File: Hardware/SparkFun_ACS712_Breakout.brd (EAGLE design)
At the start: 24.1 x 15.2 mm, 12 parts, among them U1 ACS712

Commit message: A few more QC clean ups
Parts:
- added U$1: REVISION, SparkFun-Aesthetics:REVISION
- JP1, JP2: value M01-SMTSO-256-ET -> (none); device SparkFun:SMTSO-256-ET -> SparkFun-Connectors:SMTSO-256-ET
- JP3: device SparkFun:1X04 -> SparkFun-Connectors:1X04
- JP4, JP5: device SparkFun:MICRO-FIDUCIAL -> SparkFun-Aesthetics:MICRO-FIDUCIAL
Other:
- board text added: "P. Alberts, Toni Klopfenstein"
- board text removed: "Revised by: Patrick Alberts"
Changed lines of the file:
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@@
 <?xml version="1.0" encoding="utf-8"?>
 <!DOCTYPE eagle SYSTEM "eagle.dtd">
-<eagle version="7.2.0">
+<eagle version="7.3.0">
 <drawing>
 <settings>
@@
 <layer number="45" name="Holes" color="7" fill="1" visible="yes" active="yes"/>
 <layer number="46" name="Milling" color="3" fill="1" visible="no" active="yes"/>
-<layer number="47" name="Measures" color="7" fill="1" visible="yes" active="yes"/>
+<layer number="47" name="Measures" color="7" fill="1" visible="no" active="yes"/>
 <layer number="48" name="Document" color="7" fill="1" visible="no" active="yes"/>
 <layer number="49" name="Reference" color="7" fill="1" visible="no" active="yes"/>
@@
 <layer number="113" name="IDFDebug" color="4" fill="1" visible="no" active="yes"/>
 <layer number="116" name="Patch_BOT" color="9" fill="4" visible="no" active="yes"/>
+<layer number="118" name="Rect_Pads" color="7" fill="1" visible="yes" active="yes"/>
 <layer number="121" name="_tsilk" color="7" fill="1" visible="no" active="yes"/>
 <layer number="122" name="_bsilk" color="7" fill="1" visible="no" active="yes"/>
@@
 <dimension x1="-2.54" y1="19.05" x2="21.59" y2="19.05" x3="9.525" y3="20.32" textsize="1.778" textratio="15" layer="47" unit="inch" visible="yes"/>
 <text x="7.0866" y="-10.2108" size="1.778" layer="51" font="vector">Pete Dokter</text>
-<text x="-11.43" y="-12.9794" size="1.778" layer="51" font="vector">Revised by: Patrick Alberts</text>
 <text x="16.49221875" y="11.877040625" size="0.8128" layer="22" font="vector" ratio="15" rot="MR180">VCC</text>
 <text x="18.923" y="9.271" size="0.8128" layer="21" font="vector" ratio="15" rot="R180">VOUT</text>
@@
 <text x="16.46428125" y="4.193540625" size="0.8128" layer="22" font="vector" ratio="15" rot="MR180">GND</text>
 <text x="4.699" y="0.381" size="0.8128" layer="21" font="vector" ratio="15">Max Current 13mA</text>
+<text x="7.0866" y="-12.7508" size="1.778" layer="51" font="vector">P. Alberts, Toni Klopfenstein</text>
 </plain>
 <attributes>
@@
 <attribute name="PROD_ID" value="IC-08964" x="10.287" y="7.62" size="1.778" layer="27" rot="R270" display="off"/>
 </element>
-<element name="JP1" library="SparkFun" package="SMTSO-256-ET" value="M01-SMTSO-256-ET" x="1.27" y="11.43"/>
-<element name="JP2" library="SparkFun" package="SMTSO-256-ET" value="M01-SMTSO-256-ET" x="1.27" y="3.81"/>
-<element name="JP3" library="SparkFun" package="1X04" value="" x="20.32" y="11.43" smashed="yes" rot="R270">
+<element name="JP1" library="SparkFun-Connectors" package="SMTSO-256-ET" value="" x="1.27" y="11.43"/>
+<element name="JP2" library="SparkFun-Connectors" package="SMTSO-256-ET" value="" x="1.27" y="3.81"/>
+<element name="JP3" library="SparkFun-Connectors" package="1X04" value="" x="20.32" y="11.43" smashed="yes" rot="R270">
 <attribute name="VALUE" x="17.145" y="12.7" size="1.27" layer="27" rot="R270"/>
 </element>
 <element name="U$3" library="SparkFun" package="OSHW-LOGO-S" value="OSHW-LOGOS" x="17.3482" y="13.208" rot="MR0"/>
-<element name="JP4" library="SparkFun" package="MICRO-FIDUCIAL" value="FIDUCIALUFIDUCIAL" x="20.32" y="13.97"/>
-<element name="JP5" library="SparkFun" package="MICRO-FIDUCIAL" value="FIDUCIALUFIDUCIAL" x="-1.651" y="1.016"/>
+<element name="JP4" library="SparkFun-Aesthetics" package="MICRO-FIDUCIAL" value="FIDUCIALUFIDUCIAL" x="20.32" y="13.97"/>
+<element name="JP5" library="SparkFun-Aesthetics" package="MICRO-FIDUCIAL" value="FIDUCIALUFIDUCIAL" x="-1.651" y="1.016"/>
 <element name="FRAME1" library="SparkFun-Aesthetics" package="CREATIVE_COMMONS" value="" x="-22.88245625" y="-10.16">
 <attribute name="VERSION" value="v01" x="-22.88245625" y="-10.16" size="1.778" layer="27" display="off"/>
@@
 </element>
 <element name="LOGO1" library="SparkFun-Aesthetics" package="SFE_LOGO_NAME_.1" value="SFE_LOGO_NAME.1_INCH" x="4.6736" y="10.7442"/>
+<element name="U$1" library="SparkFun-Aesthetics" package="REVISION" value="REVISION" x="-11.43" y="-12.7"/>
 </elements>
 <signals>

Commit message: Silk fix
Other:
- board text added: "+"
- board text added: "-"
- board text added: "Max Current Sensing: 5A"
- board text removed: "Max Current 13mA"
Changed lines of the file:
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@@
 <setting verticaltext="up"/>
 </settings>
-<grid distance="0.05" unitdist="inch" unit="inch" style="lines" multiple="1" display="yes" altdistance="0.005" altunitdist="inch" altunit="inch"/>
+<grid distance="0.025" unitdist="inch" unit="inch" style="lines" multiple="1" display="yes" altdistance="0.005" altunitdist="inch" altunit="inch"/>
 <layers>
 <layer number="1" name="Top" color="4" fill="1" visible="yes" active="yes"/>
@@
 <layer number="113" name="IDFDebug" color="4" fill="1" visible="no" active="yes"/>
 <layer number="116" name="Patch_BOT" color="9" fill="4" visible="no" active="yes"/>
-<layer number="118" name="Rect_Pads" color="7" fill="1" visible="yes" active="yes"/>
+<layer number="118" name="Rect_Pads" color="7" fill="1" visible="no" active="yes"/>
 <layer number="121" name="_tsilk" color="7" fill="1" visible="no" active="yes"/>
 <layer number="122" name="_bsilk" color="7" fill="1" visible="no" active="yes"/>
@@
 <text x="16.0426375" y="6.733540625" size="0.8128" layer="22" font="vector" ratio="15" rot="MR180">FILT</text>
 <text x="16.46428125" y="4.193540625" size="0.8128" layer="22" font="vector" ratio="15" rot="MR180">GND</text>
-<text x="4.699" y="0.381" size="0.8128" layer="21" font="vector" ratio="15">Max Current 13mA</text>
+<text x="3.429" y="0.381" size="0.8128" layer="21" font="vector" ratio="15">Max Current Sensing: 5A</text>
 <text x="7.0866" y="-12.7508" size="1.778" layer="51" font="vector">P. Alberts, Toni Klopfenstein</text>
+<text x="5.715" y="9.525" size="1.778" layer="21" font="vector" ratio="15">+</text>
+<text x="5.715" y="5.715" size="1.778" layer="21" font="vector" ratio="15" align="top-left">-</text>
 </plain>
 <attributes>

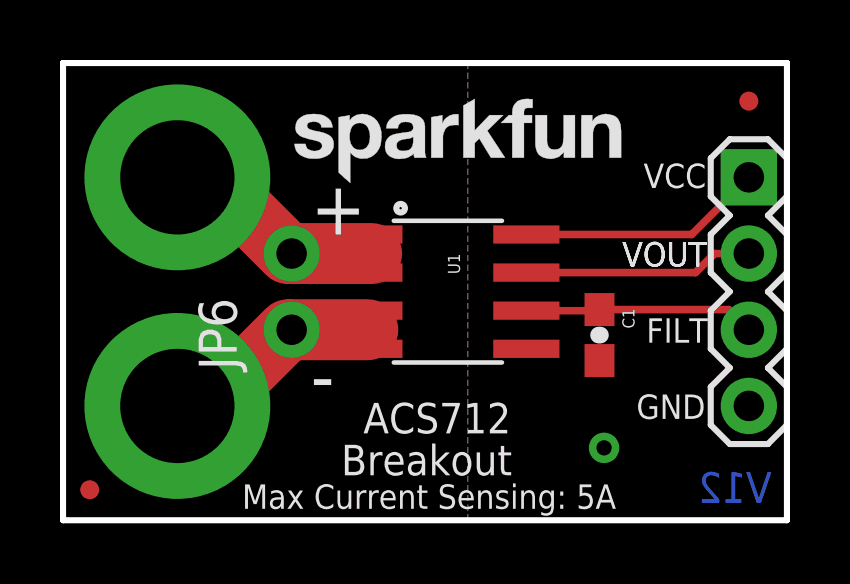
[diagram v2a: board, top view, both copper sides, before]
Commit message: Adding second trace on bottom layer
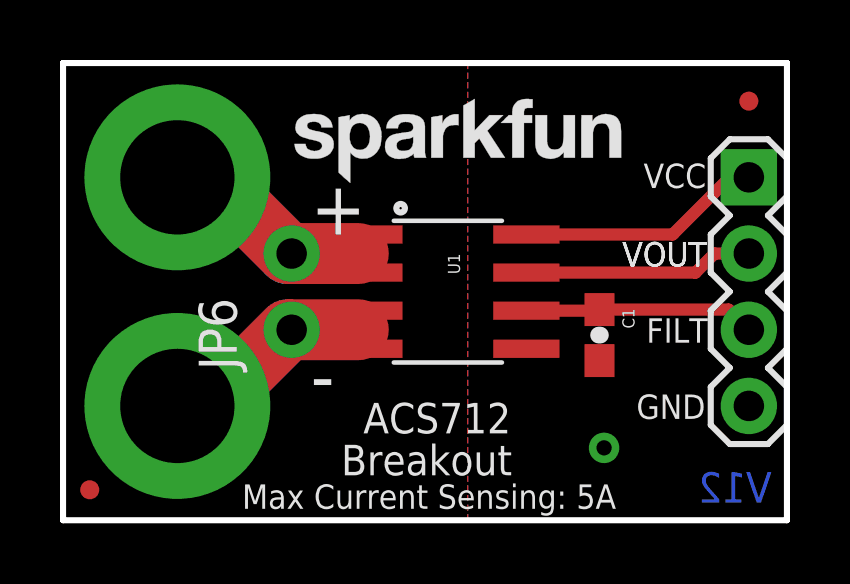
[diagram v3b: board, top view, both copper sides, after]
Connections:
- net N$1 renamed IP+
- net N$3 renamed IP-
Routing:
- net IP-: track 8.71 -> 13.4 mm
- net IP+: track 8.86 -> 13.5 mm
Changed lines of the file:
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@@
 <layer number="47" name="Measures" color="7" fill="1" visible="no" active="yes"/>
 <layer number="48" name="Document" color="7" fill="1" visible="no" active="yes"/>
-<layer number="49" name="Reference" color="7" fill="1" visible="no" active="yes"/>
+<layer number="49" name="Reference" color="7" fill="1" visible="yes" active="yes"/>
 <layer number="50" name="dxf" color="7" fill="1" visible="no" active="yes"/>
 <layer number="51" name="tDocu" color="6" fill="1" visible="yes" active="yes"/>
@@
 <text x="7.4676" y="2.8956" size="1.016" layer="21" font="vector" ratio="15">ACS712 </text>
 <text x="6.731" y="1.4986" size="1.016" layer="21" font="vector" ratio="15">Breakout</text>
-<text x="21.082" y="0.5842" size="1.016" layer="16" font="vector" ratio="15" rot="MR0">V12</text>
+<text x="21.082" y="0.5842" size="1.016" layer="16" font="vector" ratio="25" rot="MR0">V12</text>
 <dimension x1="-3.81" y1="0" x2="-3.81" y2="15.24" x3="-6.35" y3="7.62" textsize="1.778" textratio="15" layer="47" unit="inch" visible="yes"/>
 <dimension x1="-2.54" y1="19.05" x2="21.59" y2="19.05" x3="9.525" y3="20.32" textsize="1.778" textratio="15" layer="47" unit="inch" visible="yes"/>
@@
 </elements>
 <signals>
-<signal name="N$1">
+<signal name="IP+">
 <contactref element="JP1" pad="P$1"/>
 <contactref element="U1" pad="1"/>
@@
 <wire x1="2.413" y1="11.43" x2="4.953" y2="8.89" width="2.032" layer="1"/>
 <wire x1="4.953" y1="8.89" x2="5.08" y2="8.89" width="1.778" layer="1"/>
-<wire x1="5.08" y1="8.89" x2="7.747" y2="8.89" width="2.032" layer="1"/>
-<wire x1="7.6708" y1="8.9662" x2="7.6708" y2="9.525" width="0.254" layer="1"/>
-<wire x1="7.747" y1="8.89" x2="7.6708" y2="8.9662" width="0.254" layer="1"/>
-<wire x1="7.6708" y1="8.8138" x2="7.6708" y2="8.255" width="0.254" layer="1"/>
-<wire x1="7.747" y1="8.89" x2="7.6708" y2="8.8138" width="0.254" layer="1"/>
 <contactref element="JP6" pad="2"/>
-</signal>
-<signal name="N$3">
+<wire x1="5.08" y1="8.89" x2="7.3025" y2="8.89" width="2.032" layer="1"/>
+<wire x1="1.27" y1="11.43" x2="2.413" y2="11.43" width="2.032" layer="16"/>
+<wire x1="2.413" y1="11.43" x2="4.953" y2="8.89" width="2.032" layer="16"/>
+<wire x1="4.953" y1="8.89" x2="5.08" y2="8.89" width="2.032" layer="16"/>
+<wire x1="7.6708" y1="8.5217" x2="7.3025" y2="8.89" width="0.762" layer="1"/>
+<wire x1="7.6708" y1="9.2583" x2="7.3025" y2="8.89" width="0.762" layer="1"/>
+<wire x1="7.6708" y1="9.525" x2="7.6708" y2="9.2583" width="0.4064" layer="1"/>
+<wire x1="7.6708" y1="8.255" x2="7.6708" y2="8.5217" width="0.4064" layer="1"/>
+</signal>
+<signal name="IP-">
 <contactref element="U1" pad="3"/>
 <contactref element="JP2" pad="P$1"/>
@@
 <wire x1="2.413" y1="3.81" x2="4.953" y2="6.35" width="2.032" layer="1"/>
 <wire x1="4.953" y1="6.35" x2="5.08" y2="6.35" width="1.778" layer="1"/>
-<wire x1="5.08" y1="6.35" x2="7.62" y2="6.35" width="2.032" layer="1"/>
-<wire x1="7.6708" y1="6.2992" x2="7.6708" y2="5.715" width="0.254" layer="1"/>
-<wire x1="7.62" y1="6.35" x2="7.6708" y2="6.2992" width="0.254" layer="1"/>
-<wire x1="7.6708" y1="6.4008" x2="7.6708" y2="6.985" width="0.254" layer="1"/>
-<wire x1="7.62" y1="6.35" x2="7.6708" y2="6.4008" width="0.254" layer="1"/>
 <contactref element="JP6" pad="1"/>
+<wire x1="5.08" y1="6.35" x2="7.3025" y2="6.35" width="2.032" layer="1"/>
+<wire x1="1.27" y1="3.81" x2="2.413" y2="3.81" width="2.032" layer="16"/>
+<wire x1="2.413" y1="3.81" x2="4.953" y2="6.35" width="2.032" layer="16"/>
+<wire x1="7.6708" y1="6.7183" x2="7.3025" y2="6.35" width="0.762" layer="1"/>
+<wire x1="7.6708" y1="5.9817" x2="7.3025" y2="6.35" width="0.762" layer="1"/>
+<wire x1="7.6708" y1="6.985" x2="7.6708" y2="6.7183" width="0.4064" layer="1"/>
+<wire x1="7.6708" y1="5.715" x2="7.6708" y2="5.9817" width="0.4064" layer="1"/>
 </signal>
 <signal name="VCC">
 <contactref element="U1" pad="8"/>
 <contactref element="JP3" pad="1"/>
-<wire x1="12.9032" y1="9.525" x2="18.415" y2="9.525" width="0.254" layer="1"/>
-<wire x1="18.415" y1="9.525" x2="20.32" y2="11.43" width="0.254" layer="1"/>
+<wire x1="12.9032" y1="9.525" x2="17.78" y2="9.525" width="0.4064" layer="1"/>
+<wire x1="17.78" y1="9.525" x2="19.685" y2="11.43" width="0.4064" layer="1"/>
+<wire x1="19.685" y1="11.43" x2="20.32" y2="11.43" width="0.4064" layer="1"/>
 </signal>
 <signal name="VOUT">
 <contactref element="JP3" pad="2"/>
 <contactref element="U1" pad="7"/>
-<wire x1="19.177" y1="8.89" x2="20.32" y2="8.89" width="0.254" layer="1"/>
-<wire x1="18.542" y1="8.255" x2="19.177" y2="8.89" width="0.254" layer="1"/>
+<wire x1="19.177" y1="8.89" x2="20.32" y2="8.89" width="0.4064" layer="1"/>
+<wire x1="18.542" y1="8.255" x2="19.177" y2="8.89" width="0.4064" layer="1"/>
 <wire x1="12.9032" y1="8.255" x2="12.827" y2="8.255" width="0.254" layer="1"/>
-<wire x1="12.9032" y1="8.255" x2="18.542" y2="8.255" width="0.254" layer="1"/>
+<wire x1="12.9032" y1="8.255" x2="18.542" y2="8.255" width="0.4064" layer="1"/>
 </signal>
 <signal name="FILT">
@@
 <contactref element="JP3" pad="3"/>
 <contactref element="C1" pad="1"/>
-<wire x1="19.6478" y1="7.0222" x2="20.32" y2="6.35" width="0.254" layer="1"/>
-<wire x1="19.6478" y1="7.0222" x2="15.3416" y2="7.0222" width="0.254" layer="1"/>
-<wire x1="12.9032" y1="6.985" x2="15.3044" y2="6.985" width="0.254" layer="1"/>
+<wire x1="19.6478" y1="7.0222" x2="20.32" y2="6.35" width="0.4064" layer="1"/>
+<wire x1="19.6478" y1="7.0222" x2="15.3416" y2="7.0222" width="0.4064" layer="1"/>
+<wire x1="12.9032" y1="6.985" x2="15.3044" y2="6.985" width="0.4064" layer="1"/>
 <wire x1="15.3044" y1="6.985" x2="15.3416" y2="7.0222" width="0.254" layer="1"/>
 </signal>
